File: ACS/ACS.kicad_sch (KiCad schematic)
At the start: 8 parts, among them Q1 TIP120, U1 Teensy4.1, U2 TSR_1-2450, U3 BME280

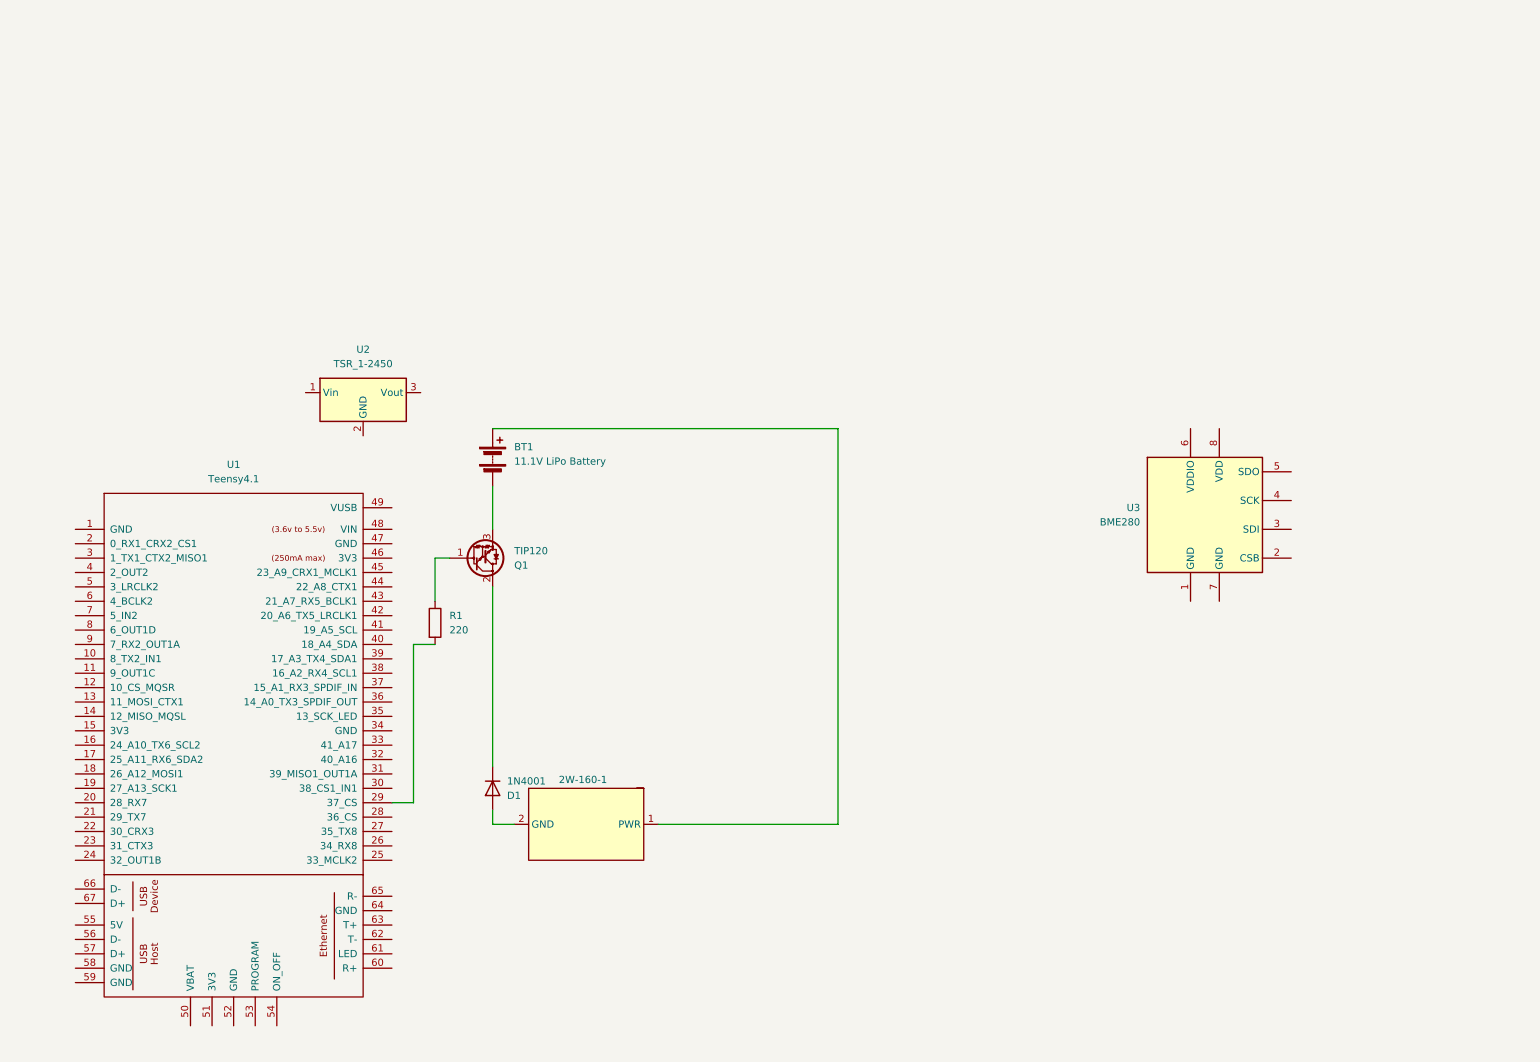
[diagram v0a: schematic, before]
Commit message: added working valve control to schematic, named folders properly
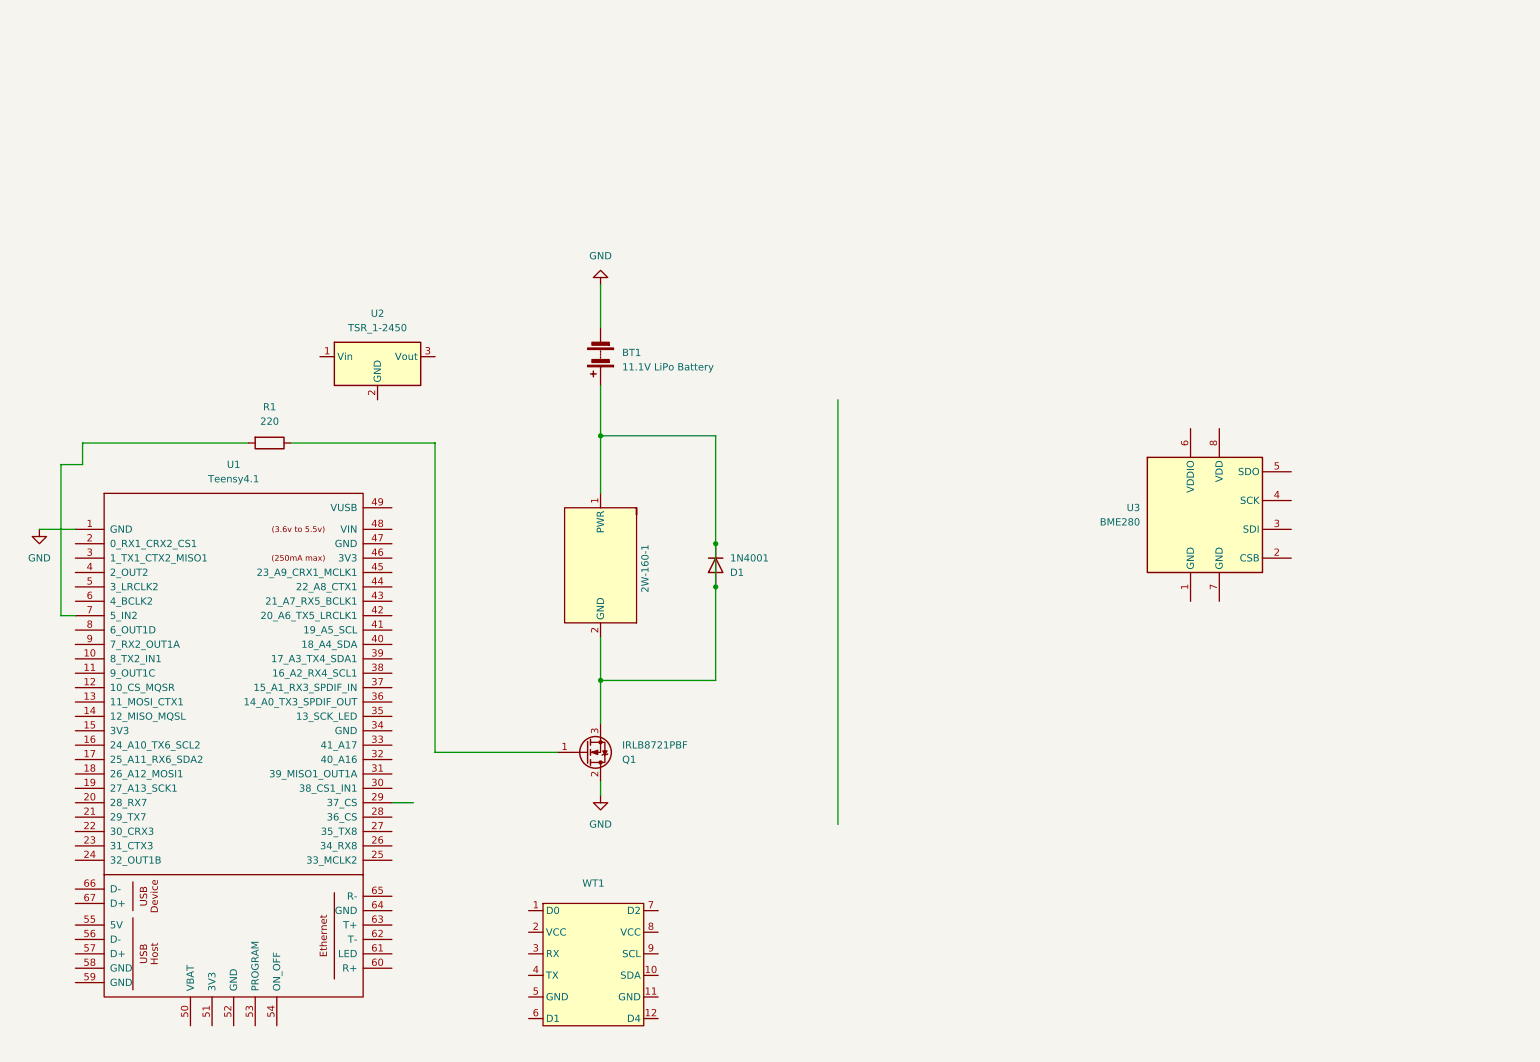
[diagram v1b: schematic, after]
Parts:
- removed Q1: TIP120, Package_TO_SOT_THT:TO-220-3_Vertical, symbol Transistor_BJT:TIP120
- added Q1: IRLB8721PBF, Package_TO_SOT_THT:TO-220-3_Vertical, symbol Transistor_FET:IRLB8721PBF
- added WT1: ~, symbol grs_comps:WT901
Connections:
- net at 2W-160-1.1 (PWR), BT1.1 (+): now also 2W-160-1.2 (GND), D1.1 (K), D1.2 (A), Q1.3 (S)
- net GND: now reaches U1.1 (GND)
- net GND: now also BT1.2 (-), Q1.2 (D)
- net at U1.29 (37_CS): no longer R1.2
- net at U1.7 (5_IN2): now also R1.2
- net at R1.1: now also Q1.1 (G)
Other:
- moved on the sheet: 2W-160-1, BT1, D1, R1, U2

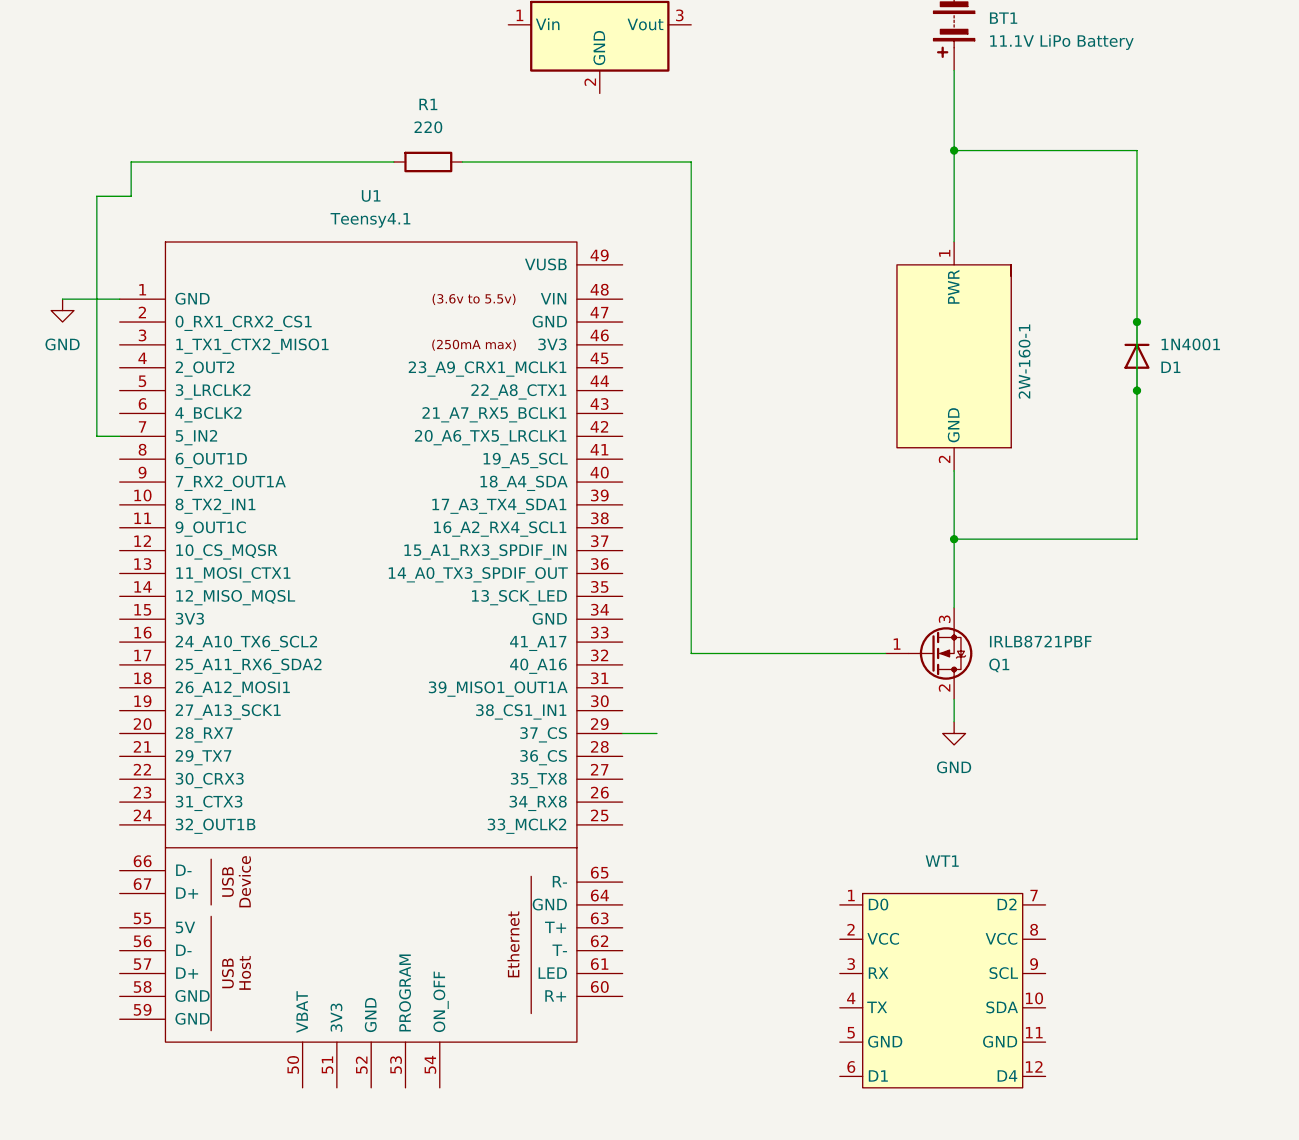
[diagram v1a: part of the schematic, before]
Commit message: IMU Wiring
Add wiring to WT901 IMU sensor
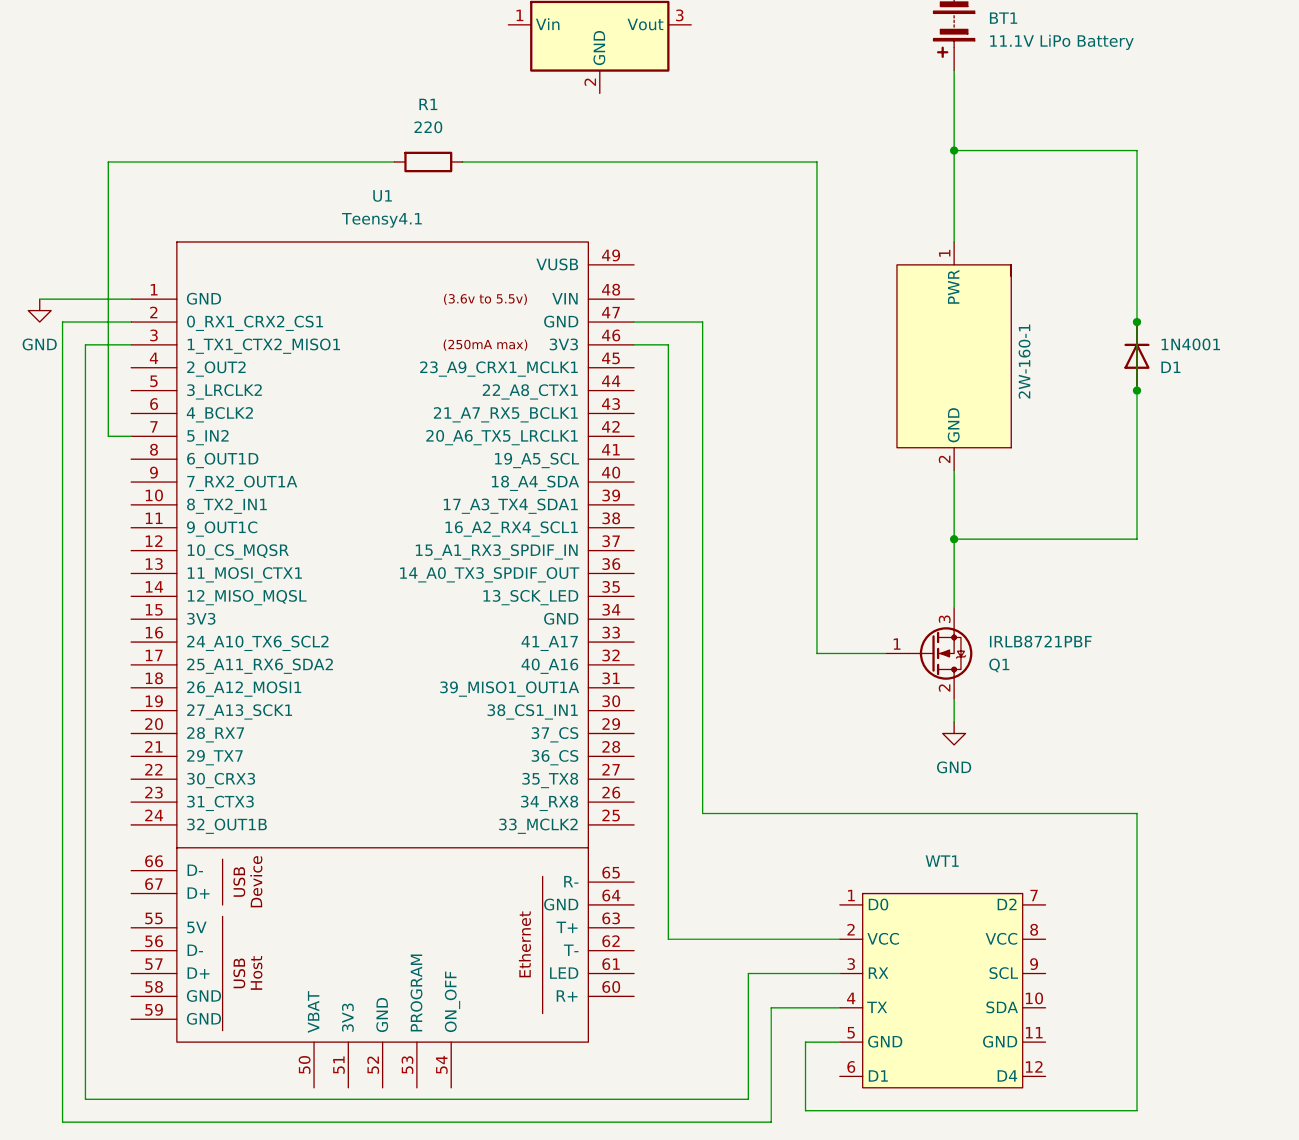
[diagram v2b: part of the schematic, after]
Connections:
- net at WT1.2 (VCC): now also U1.46 (3V3)
- net at WT1.3 (RX): now also U1.3 (1_TX1_CTX2_MISO1)
- net at WT1.4 (TX): now also U1.2 (0_RX1_CRX2_CS1)
- net at WT1.5 (GND): now also U1.47 (GND)
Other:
- moved on the sheet: U1
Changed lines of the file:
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@@
 	(wire
 		(pts
-			(xy 24.13 90.17) (xy 53.34 90.17)
-		)
-		(stroke
-			(width 0)
-			(type default)
-		)
-	)
-	(wire
-		(pts
-			(xy 20.32 120.65) (xy 22.86 120.65)
+			(xy 21.59 90.17) (xy 53.34 90.17)
+		)
+		(stroke
+			(width 0)
+			(type default)
+		)
+	)
+	(wire
+		(pts
+			(xy 19.05 110.49) (xy 24.13 110.49)
+		)
+		(stroke
+			(width 0)
+			(type default)
+		)
+	)
+	(wire
+		(pts
+			(xy 95.25 184.15) (xy 102.87 184.15)
+		)
+		(stroke
+			(width 0)
+			(type default)
+		)
+	)
+	(wire
+		(pts
+			(xy 21.59 120.65) (xy 24.13 120.65)
+		)
+		(stroke
+			(width 0)
+			(type default)
+		)
+	)
+	(wire
+		(pts
+			(xy 102.87 187.96) (xy 99.06 187.96)
 		)
 		(stroke
@@
 	(wire
 		(pts
+			(xy 16.51 107.95) (xy 16.51 196.85)
+		)
+		(stroke
+			(width 0)
+			(type default)
+		)
+	)
+	(wire
+		(pts
+			(xy 92.71 194.31) (xy 19.05 194.31)
+		)
+		(stroke
+			(width 0)
+			(type default)
+		)
+	)
+	(wire
+		(pts
+			(xy 99.06 195.58) (xy 135.89 195.58)
+		)
+		(stroke
+			(width 0)
+			(type default)
+		)
+	)
+	(wire
+		(pts
 			(xy 135.89 132.08) (xy 135.89 115.57)
 		)
@@
 	(wire
 		(pts
-			(xy 24.13 93.98) (xy 24.13 90.17)
+			(xy 16.51 107.95) (xy 24.13 107.95)
+		)
+		(stroke
+			(width 0)
+			(type default)
+		)
+	)
+	(wire
+		(pts
+			(xy 95.25 196.85) (xy 16.51 196.85)
+		)
+		(stroke
+			(width 0)
+			(type default)
+		)
+	)
+	(wire
+		(pts
+			(xy 19.05 194.31) (xy 19.05 110.49)
 		)
 		(stroke
@@
 	(wire
 		(pts
+			(xy 83.82 110.49) (xy 80.01 110.49)
+		)
+		(stroke
+			(width 0)
+			(type default)
+		)
+	)
+	(wire
+		(pts
 			(xy 115.57 132.08) (xy 135.89 132.08)
 		)
@@
 	(wire
 		(pts
-			(xy 16.51 105.41) (xy 22.86 105.41)
-		)
-		(stroke
-			(width 0)
-			(type default)
-		)
-	)
-	(wire
-		(pts
-			(xy 82.55 153.67) (xy 78.74 153.67)
+			(xy 87.63 107.95) (xy 80.01 107.95)
+		)
+		(stroke
+			(width 0)
+			(type default)
+		)
+	)
+	(wire
+		(pts
+			(xy 13.97 105.41) (xy 24.13 105.41)
+		)
+		(stroke
+			(width 0)
+			(type default)
+		)
+	)
+	(wire
+		(pts
+			(xy 99.06 187.96) (xy 99.06 195.58)
 		)
 		(stroke
@@
 	(wire
 		(pts
-			(xy 20.32 93.98) (xy 20.32 120.65)
-		)
-		(stroke
-			(width 0)
-			(type default)
-		)
-	)
-	(wire
-		(pts
-			(xy 86.36 144.78) (xy 86.36 90.17)
+			(xy 135.89 162.56) (xy 87.63 162.56)
+		)
+		(stroke
+			(width 0)
+			(type default)
+		)
+	)
+	(wire
+		(pts
+			(xy 21.59 90.17) (xy 21.59 120.65)
+		)
+		(stroke
+			(width 0)
+			(type default)
+		)
+	)
+	(wire
+		(pts
+			(xy 100.33 144.78) (xy 100.33 90.17)
+		)
+		(stroke
+			(width 0)
+			(type default)
+		)
+	)
+	(wire
+		(pts
+			(xy 135.89 195.58) (xy 135.89 162.56)
 		)
 		(stroke
@@
 	(wire
 		(pts
-			(xy 86.36 90.17) (xy 60.96 90.17)
-		)
-		(stroke
-			(width 0)
-			(type default)
-		)
-	)
-	(wire
-		(pts
-			(xy 20.32 93.98) (xy 24.13 93.98)
-		)
-		(stroke
-			(width 0)
-			(type default)
-		)
-	)
-	(wire
-		(pts
-			(xy 86.36 144.78) (xy 107.95 144.78)
+			(xy 100.33 90.17) (xy 60.96 90.17)
+		)
+		(stroke
+			(width 0)
+			(type default)
+		)
+	)
+	(wire
+		(pts
+			(xy 102.87 176.53) (xy 83.82 176.53)
+		)
+		(stroke
+			(width 0)
+			(type default)
+		)
+	)
+	(wire
+		(pts
+			(xy 100.33 144.78) (xy 107.95 144.78)
 		)
 		(stroke
@@
 	(wire
 		(pts
+			(xy 92.71 180.34) (xy 92.71 194.31)
+		)
+		(stroke
+			(width 0)
+			(type default)
+		)
+	)
+	(wire
+		(pts
 			(xy 115.57 80.01) (xy 115.57 88.9)
+		)
+		(stroke
+			(width 0)
+			(type default)
+		)
+	)
+	(wire
+		(pts
+			(xy 95.25 184.15) (xy 95.25 196.85)
+		)
+		(stroke
+			(width 0)
+			(type default)
+		)
+	)
+	(wire
+		(pts
+			(xy 102.87 180.34) (xy 92.71 180.34)
+		)
+		(stroke
+			(width 0)
+			(type default)
+		)
+	)
+	(wire
+		(pts
+			(xy 87.63 162.56) (xy 87.63 107.95)
+		)
+		(stroke
+			(width 0)
+			(type default)
+		)
+	)
+	(wire
+		(pts
+			(xy 83.82 110.49) (xy 83.82 176.53)
 		)
 		(stroke
@@
 	(symbol
 		(lib_id "teensy:Teensy4.1")
-		(at 50.8 160.02 0)
+		(at 52.07 160.02 0)
 		(unit 1)
 		(exclude_from_sim no)
@@
 		(fields_autoplaced yes)
 		(property "Reference" "U1"
-			(at 50.8 93.98 0)
+			(at 52.07 93.98 0)
 			(effects
 				(font
@@
 		)
 		(property "Value" "Teensy4.1"
-			(at 50.8 96.52 0)
+			(at 52.07 96.52 0)
 			(effects
 				(font
@@
 		)
 		(property "Footprint" ""
-			(at 40.64 149.86 0)
+			(at 41.91 149.86 0)
 			(effects
 				(font
@@
 		)
 		(property "Datasheet" ""
-			(at 40.64 149.86 0)
+			(at 41.91 149.86 0)
 			(effects
 				(font
@@
 		)
 		(property "Description" ""
-			(at 50.8 160.02 0)
+			(at 52.07 160.02 0)
 			(effects
 				(font
@@
 	(symbol
 		(lib_id "power:GND")
-		(at 16.51 105.41 0)
+		(at 13.97 105.41 0)
 		(unit 1)
 		(exclude_from_sim no)
@@
 		(fields_autoplaced yes)
 		(property "Reference" "#PWR01"
-			(at 16.51 111.76 0)
+			(at 13.97 111.76 0)
 			(effects
 				(font
@@
 		)
 		(property "Value" "GND"
-			(at 16.51 110.49 0)
+			(at 13.97 110.49 0)
 			(effects
 				(font
@@
 		)
 		(property "Footprint" ""
-			(at 16.51 105.41 0)
+			(at 13.97 105.41 0)
 			(effects
 				(font
@@
 		)
 		(property "Datasheet" ""
-			(at 16.51 105.41 0)
+			(at 13.97 105.41 0)
 			(effects
 				(font
@@
 		)
 		(property "Description" "Power symbol creates a global label with name \"GND\" , ground"
-			(at 16.51 105.41 0)
-			(effects
-				(font
+			(at 13.97 105.41 0)
+			(effects
+				(font
